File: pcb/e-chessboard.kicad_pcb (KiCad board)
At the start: 4 copper layers, 170 x 170 mm, 66 parts, among them J1 POWER, J2 UART, Q1 BC847, Q2 BC847, SW1 Reset, SW2 Boot, U1 ESP32-WROOM-32U, U10 MAGNET_LDR, U11 MAGNET_LDR, U12 MAGNET_LDR, U13 NCV7608, U2 AOZ1280, U3 NCV7608, U4 MAGNET_LDR, U5 MAGNET_LDR, U6 MAGNET_LDR, U7 MAGNET_LDR, U8 MAGNET_LDR, U9 MAGNET_LDR

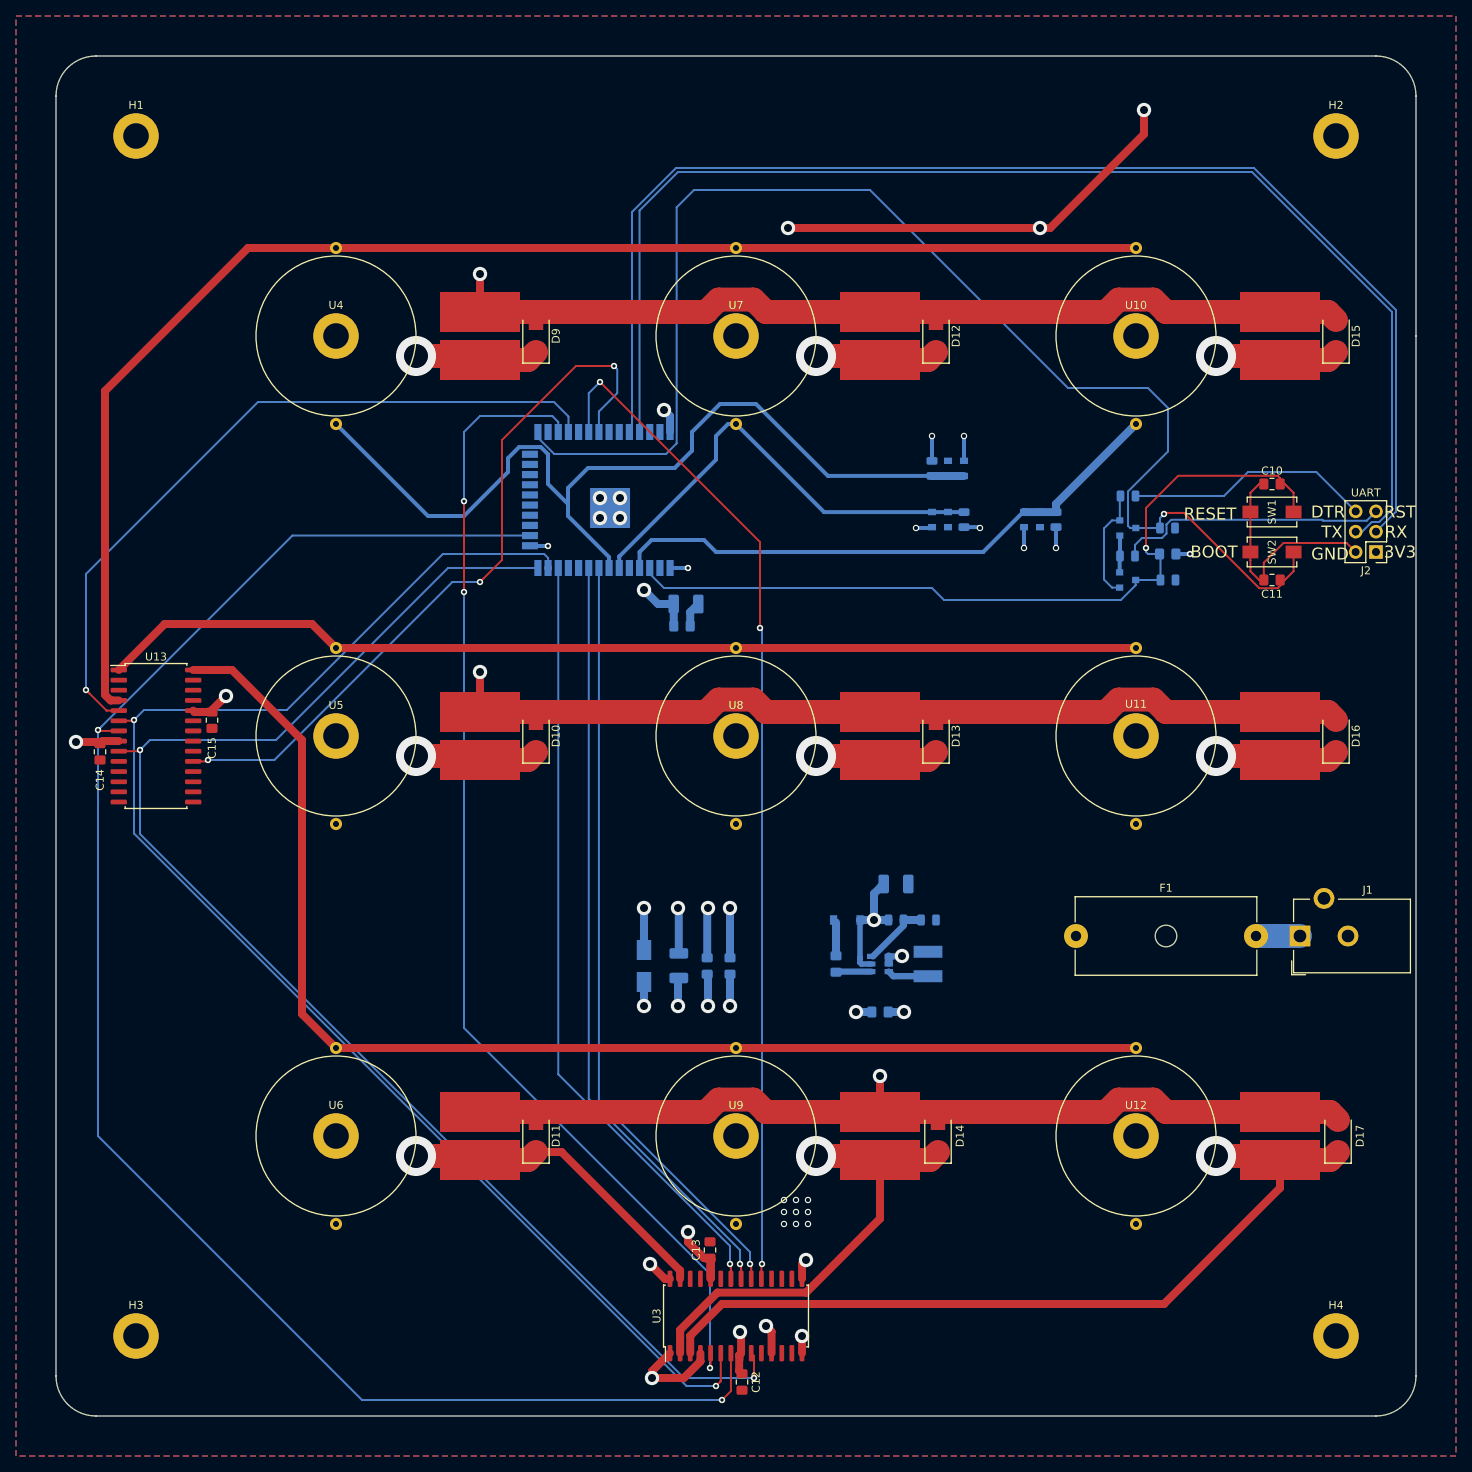
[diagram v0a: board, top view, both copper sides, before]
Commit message: feat(kicad): switching to 2 layer board
Deleting every compoenent and switching from 4 layer to 2 layer.
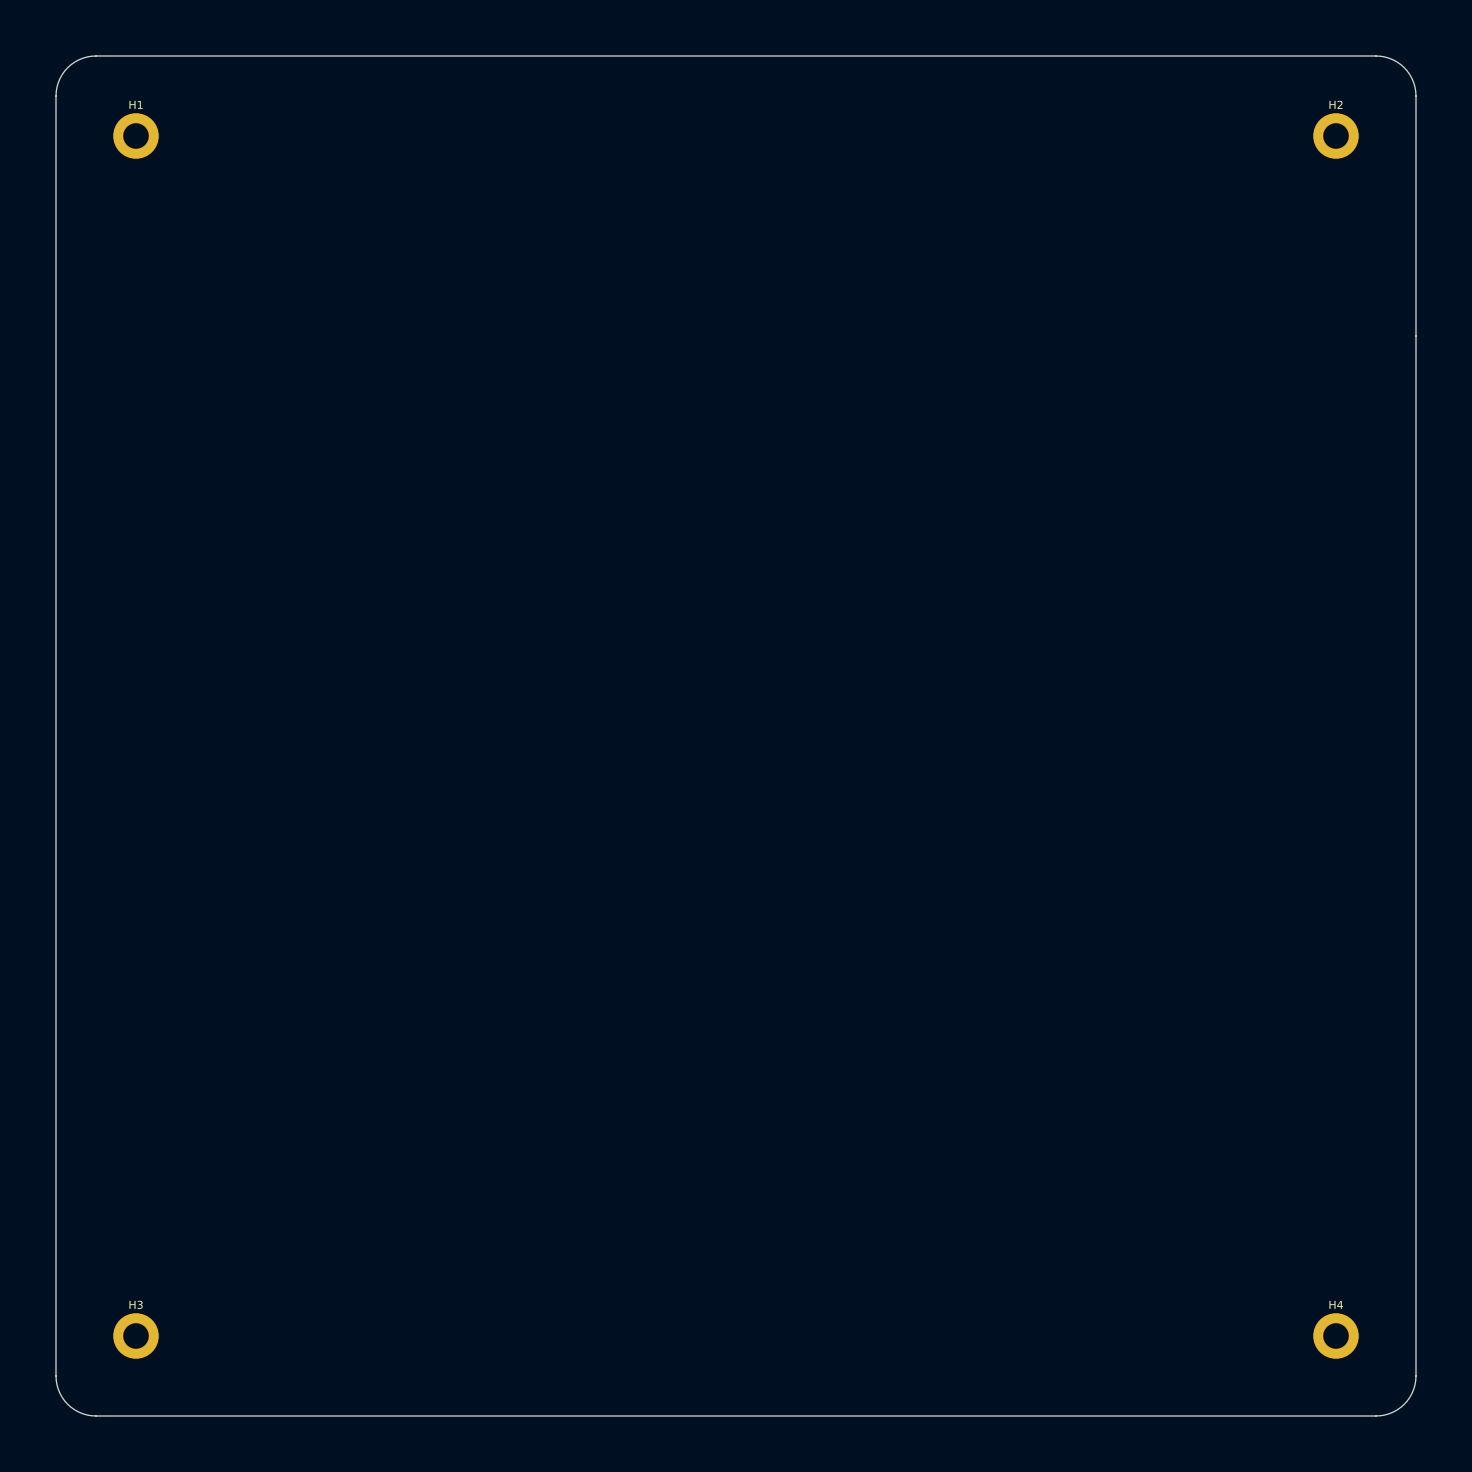
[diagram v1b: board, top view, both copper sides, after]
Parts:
- removed C1, C3, C8: 10u, Capacitor_Tantalum_SMD:CP_EIA-3528-21_Kemet-B
- removed C10, C11, C13, C15, C9: 100nF, Capacitor_SMD:C_0805_2012Metric_Pad1.15x1.40mm_HandSolder
- removed C12, C14, C2, C4: 100n, Capacitor_SMD:C_0805_2012Metric_Pad1.15x1.40mm_HandSolder
- removed C5, C7: 10n, Capacitor_SMD:C_0805_2012Metric_Pad1.15x1.40mm_HandSolder
- removed C6: 4.7u, Capacitor_SMD:C_0805_2012Metric_Pad1.15x1.40mm_HandSolder
- removed D1, D2, D4, D5, D6, D7: D_Zener, Diode_SMD:D_SOD-110
- removed D10, D11, D12, D13, D14, D15, D16, D17, D9: D, Diode_SMD:D_SMA
- removed D3: D_Zener, Diode_SMD:D_SMA
- removed D8: D_Schottky, Diode_SMD:D_SOD-123
- removed F1: Fuse, Fuse:Fuseholder_Cylinder-5x20mm_Schurter_0031_8201_Horizontal_Open
- removed J1: POWER, Connector_BarrelJack:BarrelJack_CUI_PJ-102AH_Horizontal
- removed J2: UART, Connector_PinHeader_2.54mm:PinHeader_2x03_P2.54mm_Vertical
- removed L1: 2.2uH, Inductor_SMD:L_Bourns-SRN4018
- removed Q1, Q2: BC847, Package_TO_SOT_SMD:SOT-23
- removed R1, R2, R5, R6: 10k, Resistor_SMD:R_0805_2012Metric
- removed R3: 49.9k, Resistor_SMD:R_0805_2012Metric
- removed R4: 15.8k, Resistor_SMD:R_0805_2012Metric
- removed R7, R8, R9: 300k, Resistor_SMD:R_0805_2012Metric
- removed SW1: Reset, Button_Switch_SMD:SW_SPST_EVQPE1
- removed SW2: Boot, Button_Switch_SMD:SW_SPST_EVQPE1
- removed U1: ESP32-WROOM-32U, RF_Module:ESP32-WROOM-32U
- removed U10, U11, U12, U4, U5, U6, U7, U8, U9: MAGNET_LDR, lib_fp:20_15_electromagnet_ldr
- removed U13, U3: NCV7608, Package_SO:SOIC-28W_7.5x17.9mm_P1.27mm
- removed U2: AOZ1280, Package_TO_SOT_SMD:SOT-23-6
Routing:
- net MAG_ROW_1: track 326.7 -> 0.00 mm, vias 2 -> 0
- net MAG_COL_1: track 234.2 -> 0.00 mm, vias 3 -> 0
- net MAG_ROW_2: track 231.9 -> 0.00 mm, vias 2 -> 0
- net LDR_ADC1: track 220.6 -> 0.00 mm
- net MOSI: track 215.4 -> 0.00 mm, vias 2 -> 0
- net MAG_COL_2: track 188.1 -> 0.00 mm, vias 3 -> 0
- net SCLK: track 183.7 -> 0.00 mm, vias 2 -> 0
- net LDR_ADC3: track 180.6 -> 0.00 mm
- net MISO: track 180.5 -> 0.00 mm, vias 2 -> 0
- net LDR_ROW1: track 176.3 -> 0.00 mm
- net MAG_COL_3: track 172.0 -> 0.00 mm, vias 3 -> 0
- net IO0: track 169.3 -> 0.00 mm, vias 1 -> 0
- net LDR_ADC2: track 165.5 -> 0.00 mm
- net UART_RX: track 161.5 -> 0.00 mm
- net UART_TX: track 161.3 -> 0.00 mm
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- removed copper zone on In1.Cu, net +12V
- removed copper zone on B.Cu, net +3V3
- removed copper zone on F.Cu, net GND
- removed copper zone on In2.Cu, net GND
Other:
- board text removed: "3V3"
- board text removed: "BOOT"
- board text removed: "DTR"
- board text removed: "GND"
- board text removed: "RESET"
- board text removed: "RST"
- board text removed: "RX"
- board text removed: "TX"

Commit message: feat(kicad): placing all components and drawing wires
Placing all components and laying the wires for the 3x3 magnet matrix.
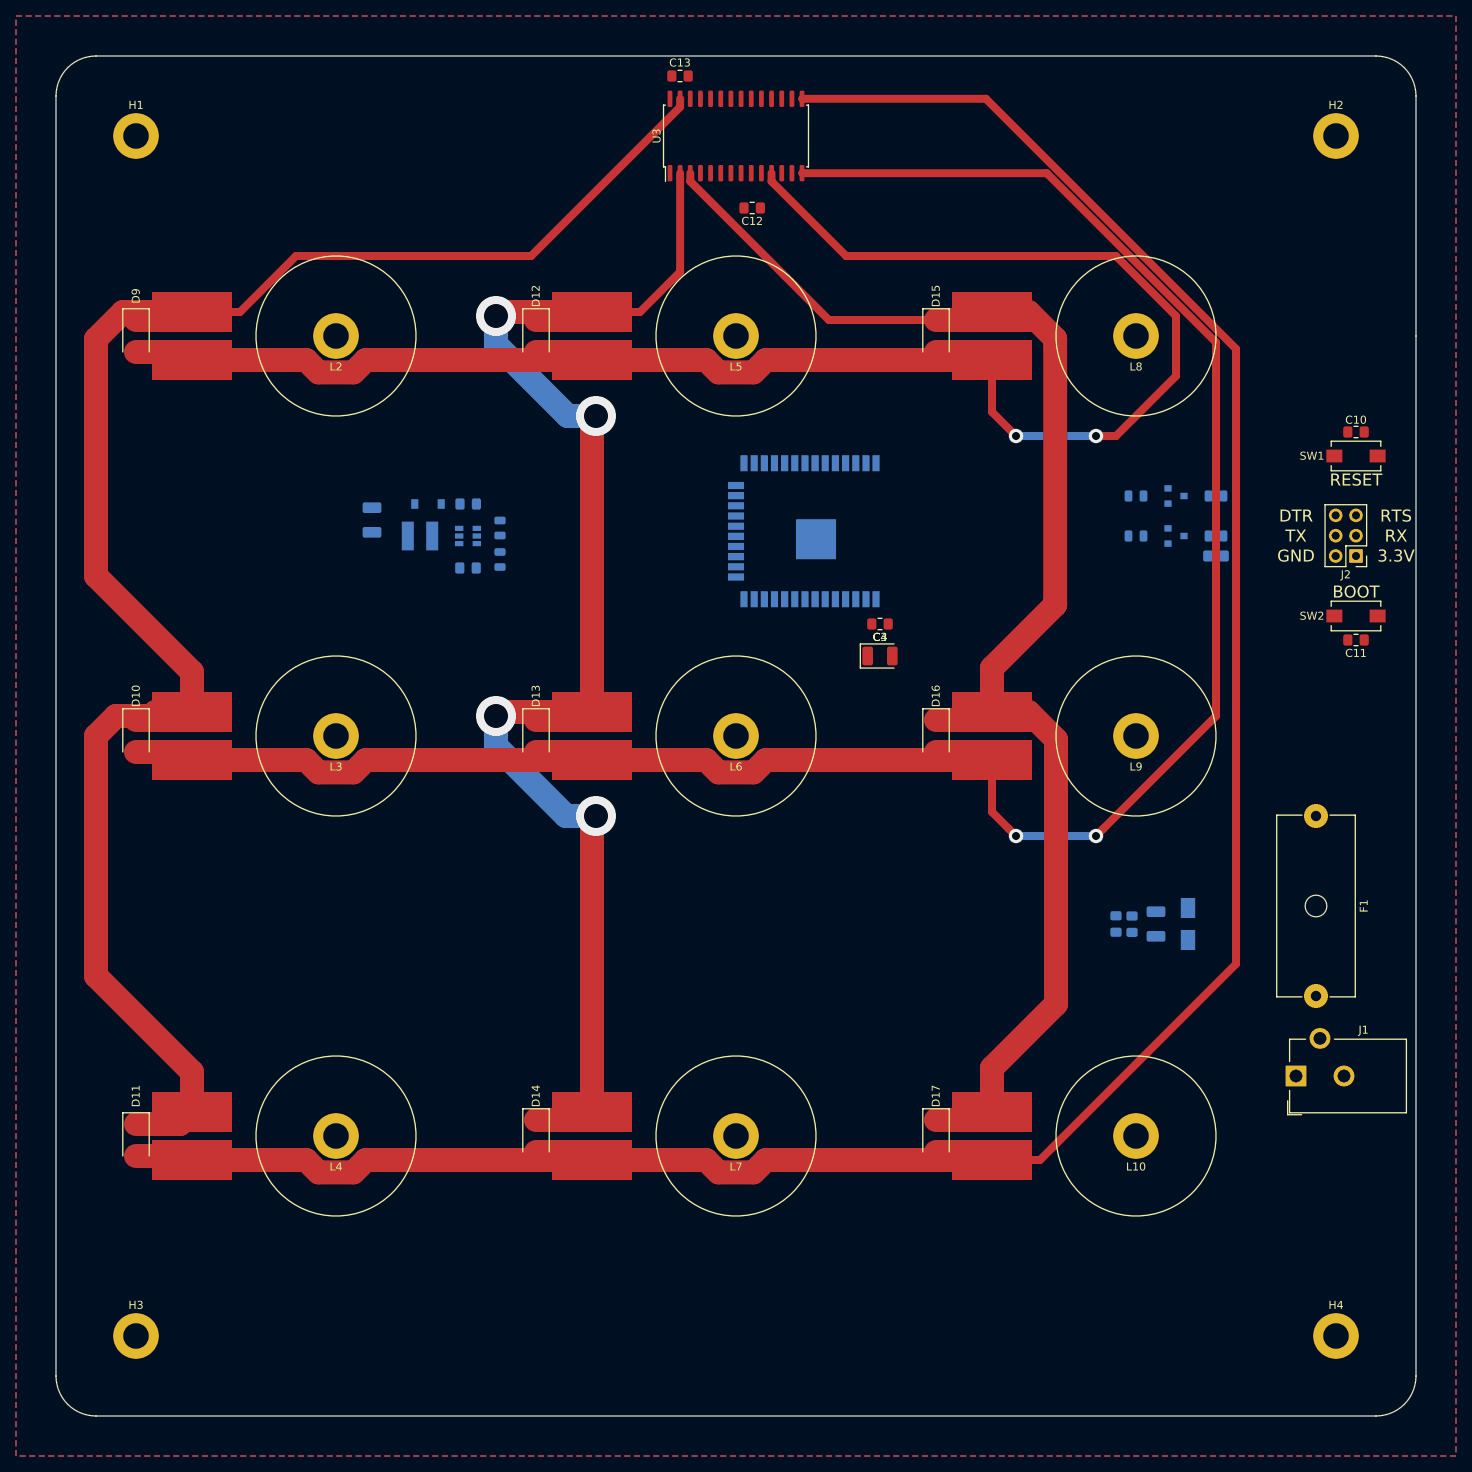
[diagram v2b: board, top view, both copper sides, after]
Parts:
- added C1: 10u, Capacitor_Tantalum_SMD:CP_EIA-3528-21_Kemet-B, B.Cu at (187.5, 158.5)
- added C10: 100nF, Capacitor_SMD:C_0805_2012Metric_Pad1.15x1.40mm_HandSolder, F.Cu at (212.5, 97.0)
- added C11: 100nF, Capacitor_SMD:C_0805_2012Metric_Pad1.15x1.40mm_HandSolder, F.Cu at (212.5, 123.0)
- added C12: 100n, Capacitor_SMD:C_0805_2012Metric_Pad1.15x1.40mm_HandSolder, F.Cu at (137.0, 69.0)
- added C13: 100nF, Capacitor_SMD:C_0805_2012Metric_Pad1.15x1.40mm_HandSolder, F.Cu at (128.0, 52.5)
- added C2: 100n, Capacitor_SMD:C_0805_2012Metric_Pad1.15x1.40mm_HandSolder, B.Cu at (184.5, 158.5)
- added C3: 10u, Capacitor_Tantalum_SMD:CP_EIA-3528-21_Kemet-B, F.Cu at (153.0, 125.0)
- added C4: 100n, Capacitor_SMD:C_0805_2012Metric_Pad1.15x1.40mm_HandSolder, F.Cu at (153.0, 121.0)
- added C5: 10n, Capacitor_SMD:C_0805_2012Metric_Pad1.15x1.40mm_HandSolder, B.Cu at (182.5, 158.5)
- added C6: 4.7u, Capacitor_SMD:C_0805_2012Metric_Pad1.15x1.40mm_HandSolder, B.Cu at (101.5, 114.0)
- added C7: 10n, Capacitor_SMD:C_0805_2012Metric_Pad1.15x1.40mm_HandSolder, B.Cu at (101.5, 106.0)
- added C8: 10u, Capacitor_Tantalum_SMD:CP_EIA-3528-21_Kemet-B, B.Cu at (89.5, 108.0)
- added C9: 100nF, Capacitor_SMD:C_0805_2012Metric_Pad1.15x1.40mm_HandSolder, B.Cu at (195.0, 112.5)
- added D10: D, Diode_SMD:D_SMA, F.Cu at (60.0, 135.0)
- added D11: D, Diode_SMD:D_SMA, F.Cu at (60.0, 185.5)
- added D12: D, Diode_SMD:D_SMA, F.Cu at (110.0, 85.0)
- added D13: D, Diode_SMD:D_SMA, F.Cu at (110.0, 135.0)
- added D14: D, Diode_SMD:D_SMA, F.Cu at (110.0, 185.0)
- added D15: D, Diode_SMD:D_SMA, F.Cu at (160.0, 85.0)
- added D16: D, Diode_SMD:D_SMA, F.Cu at (160.0, 135.0)
- added D17: D, Diode_SMD:D_SMA, F.Cu at (160.0, 185.0)
- added D3: D_Zener, Diode_SMD:D_SMA, B.Cu at (191.5, 158.5)
- added D8: D_Schottky, Diode_SMD:D_SOD-123, B.Cu at (96.5, 106.0)
- added D9: D, Diode_SMD:D_SMA, F.Cu at (60.0, 85.0)
- added F1: Fuse, Fuse:Fuseholder_Cylinder-5x20mm_Schurter_0031_8201_Horizontal_Open, F.Cu at (207.5, 145.0)
- added J1: POWER, Connector_BarrelJack:BarrelJack_CUI_PJ-102AH_Horizontal, F.Cu at (205.0, 177.5)
- added J2: UART, Connector_PinHeader_2.54mm:PinHeader_2x03_P2.54mm_Vertical, F.Cu at (212.5, 112.5)
- added L1: 2.2uH, Inductor_SMD:L_Bourns-SRN4018, B.Cu at (95.5, 110.0)
- added L10: INDUCTOR, lib_fp:20_15_electromagnet, F.Cu at (185.0, 185.0)
- added L2: INDUCTOR, lib_fp:20_15_electromagnet, F.Cu at (85.0, 85.0)
- added L3: INDUCTOR, lib_fp:20_15_electromagnet, F.Cu at (85.0, 135.0)
- added L4: INDUCTOR, lib_fp:20_15_electromagnet, F.Cu at (85.0, 185.0)
- added L5: INDUCTOR, lib_fp:20_15_electromagnet, F.Cu at (135.0, 85.0)
- added L6: INDUCTOR, lib_fp:20_15_electromagnet, F.Cu at (135.0, 135.0)
- added L7: INDUCTOR, lib_fp:20_15_electromagnet, F.Cu at (135.0, 185.0)
- added L8: INDUCTOR, lib_fp:20_15_electromagnet, F.Cu at (185.0, 85.0)
- added L9: INDUCTOR, lib_fp:20_15_electromagnet, F.Cu at (185.0, 135.0)
- added Q1: BC847, Package_TO_SOT_SMD:SOT-23, B.Cu at (190.0, 110.0)
- added Q2: BC847, Package_TO_SOT_SMD:SOT-23, B.Cu at (190.0, 105.0)
- added R1: 10k, Resistor_SMD:R_0805_2012Metric, B.Cu at (185.0, 110.0)
- added R2: 10k, Resistor_SMD:R_0805_2012Metric, B.Cu at (185.0, 105.0)
- added R3: 49.9k, Resistor_SMD:R_0805_2012Metric, B.Cu at (105.5, 112.9)
- added R4: 15.8k, Resistor_SMD:R_0805_2012Metric, B.Cu at (105.5, 109.0)
- added R5: 10k, Resistor_SMD:R_0805_2012Metric, B.Cu at (195.0, 110.0)
- added R6: 10k, Resistor_SMD:R_0805_2012Metric, B.Cu at (195.0, 105.0)
- added SW1: Reset, Button_Switch_SMD:SW_SPST_EVQPE1, F.Cu at (212.5, 100.0)
- added SW2: Boot, Button_Switch_SMD:SW_SPST_EVQPE1, F.Cu at (212.5, 120.0)
- added U1: ESP32-WROOM-32U, RF_Module:ESP32-WROOM-32U, B.Cu at (144.3, 109.4)
- added U2: AOZ1280, Package_TO_SOT_SMD:SOT-23-6, B.Cu at (101.5, 110.0)
- added U3: NCV7608, Package_SO:SOIC-28W_7.5x17.9mm_P1.27mm, F.Cu at (135.0, 60.0)
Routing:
- net MAG_ROW_3: track 0.00 -> 309.3 mm
- net MAG_ROW_2: track 0.00 -> 274.0 mm, vias 0 -> 2
- net MAG_ROW_1: track 0.00 -> 232.6 mm, vias 0 -> 2
- net MAG_COL_3: track 0.00 -> 225.3 mm
- net MAG_COL_2: track 0.00 -> 186.1 mm, vias 0 -> 4
- net MAG_COL_1: track 0.00 -> 179.7 mm
- added copper zone on B.Cu, net GND
- added copper zone on F.Cu, net GND
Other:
- copper layers 4 -> 2
- board text added: "3.3V"
- board text added: "BOOT"
- board text added: "DTR"
- board text added: "GND"
- board text added: "RESET"
- board text added: "RTS"
- board text added: "RX"
- board text added: "TX"
